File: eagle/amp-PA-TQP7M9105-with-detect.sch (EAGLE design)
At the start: 44 parts, among them J1 142-0701-851, J2 142-0701-851, Q1 P-CH, Q2 N-CH, U1 TQP7M9105, U2 BDCN-20-13+, U3 LT5534, U4 LT5534

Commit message: Update UHF PA board
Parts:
- added JP6: NP, oresat-rcl:R-US_0603-B-NOSILK
- added R9: 0, oresat-rcl:R-US_0603-B-NOSILK
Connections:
- removed net N$10: JP1.2, R7.2, U3.EN, U4.EN
- new net N$11: JP1.2, R7.2, R9.2
- new net N$14: JP6.2, R9.1, U3.EN, U4.EN
- net N$25: now also JP6.1
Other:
- note added: "2"
- note added: "Jumper"
- note added: "Optional LPF Refer to LT5534 datasheet"
- note added: "Thermal connection to ground planes are required. Dissipates up to 1W of heat."
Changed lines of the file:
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@@
 <part name="JP2" library="pinhead" library_urn="urn:adsk.eagle:library:325" deviceset="PINHD-1X3" device="" package3d_urn="urn:adsk.eagle:package:22458/2"/>
 <part name="GND11" library="supply1" library_urn="urn:adsk.eagle:library:371" deviceset="GND" device=""/>
+<part name="JP6" library="oresat-rcl" deviceset="R-US_" device="0603-B-NOSILK" value="NP"/>
+<part name="R9" library="oresat-rcl" deviceset="R-US_" device="0603-B-NOSILK" value="0"/>
 </parts>
 <sheets>
@@
 <text x="21.59" y="187.96" size="1.778" layer="97" align="bottom-right">5.0V
 External</text>
+<text x="185.42" y="170.18" size="1.778" layer="97">Optional LPF
+Refer to LT5534 datasheet</text>
+<text x="58.42" y="26.67" size="1.778" layer="97">Thermal connection to ground
+planes are required.  Dissipates
+up to 1W of heat.</text>
+<wire x1="81.28" y1="194.31" x2="99.06" y2="194.31" width="0.1524" layer="97" style="shortdash"/>
+<wire x1="99.06" y1="194.31" x2="99.06" y2="176.53" width="0.1524" layer="97" style="shortdash"/>
+<wire x1="99.06" y1="176.53" x2="81.28" y2="176.53" width="0.1524" layer="97" style="shortdash"/>
+<wire x1="81.28" y1="176.53" x2="81.28" y2="194.31" width="0.1524" layer="97" style="shortdash"/>
+<text x="82.55" y="191.77" size="1.778" layer="97">Jumper</text>
+<text x="95.25" y="190.5" size="1.778" layer="97">1</text>
+<text x="83.82" y="182.88" size="1.778" layer="97">2</text>
 </plain>
 <instances>
@@
 </instance>
 <instance part="JP4" gate="G$1" x="46.99" y="190.5" smashed="yes" rot="R180">
-<attribute name="NAME" x="54.61" y="184.785" size="1.778" layer="95" rot="R180"/>
+<attribute name="NAME" x="54.61" y="179.705" size="1.778" layer="95" rot="R180"/>
 <attribute name="VALUE" x="53.34" y="195.58" size="1.778" layer="96" rot="R180"/>
 </instance>
@@
 <instance part="GND11" gate="1" x="133.35" y="184.15" smashed="yes">
 <attribute name="VALUE" x="130.81" y="181.61" size="1.778" layer="96"/>
+</instance>
+<instance part="JP6" gate="R" x="88.9" y="181.61" smashed="yes">
+<attribute name="NAME" x="82.55" y="188.1886" size="1.778" layer="95"/>
+<attribute name="VALUE" x="85.09" y="178.308" size="1.778" layer="96"/>
+</instance>
+<instance part="R9" gate="R" x="93.98" y="186.69" smashed="yes" rot="R90">
+<attribute name="VALUE" x="97.282" y="182.88" size="1.778" layer="96" rot="R90"/>
 </instance>
 </instances>
@@
 <wire x1="101.6" y1="161.29" x2="129.54" y2="161.29" width="0.1524" layer="91"/>
 <junction x="129.54" y="161.29"/>
-</segment>
-</net>
-<net name="N$10" class="0">
-<segment>
-<pinref part="U3" gate="G$1" pin="EN"/>
-<wire x1="116.84" y1="186.69" x2="116.84" y2="168.91" width="0.1524" layer="91"/>
-<wire x1="116.84" y1="168.91" x2="147.32" y2="168.91" width="0.1524" layer="91"/>
-<wire x1="116.84" y1="168.91" x2="116.84" y2="134.62" width="0.1524" layer="91"/>
-<wire x1="116.84" y1="134.62" x2="170.18" y2="134.62" width="0.1524" layer="91"/>
-<junction x="116.84" y="168.91"/>
-<pinref part="U4" gate="G$1" pin="EN"/>
-<wire x1="170.18" y1="134.62" x2="170.18" y2="123.19" width="0.1524" layer="91"/>
-<wire x1="170.18" y1="123.19" x2="175.26" y2="123.19" width="0.1524" layer="91"/>
-<pinref part="R7" gate="R" pin="2"/>
-<wire x1="121.92" y1="185.42" x2="121.92" y2="186.69" width="0.1524" layer="91"/>
-<wire x1="121.92" y1="186.69" x2="116.84" y2="186.69" width="0.1524" layer="91"/>
-<pinref part="JP1" gate="A" pin="2"/>
-<wire x1="133.35" y1="193.04" x2="116.84" y2="193.04" width="0.1524" layer="91"/>
-<wire x1="116.84" y1="193.04" x2="116.84" y2="186.69" width="0.1524" layer="91"/>
-<junction x="116.84" y="186.69"/>
 </segment>
 </net>
@@
 <wire x1="60.96" y1="87.63" x2="60.96" y2="88.9" width="0.1524" layer="91"/>
 <pinref part="JP2" gate="A" pin="2"/>
-<wire x1="36.83" y1="88.9" x2="60.96" y2="88.9" width="0.1524" layer="91"/>
+<wire x1="36.83" y1="88.9" x2="58.42" y2="88.9" width="0.1524" layer="91"/>
 <junction x="60.96" y="88.9"/>
-</segment>
-</net>
+<pinref part="JP6" gate="R" pin="1"/>
+<wire x1="58.42" y1="88.9" x2="60.96" y2="88.9" width="0.1524" layer="91"/>
+<wire x1="83.82" y1="181.61" x2="58.42" y2="181.61" width="0.1524" layer="91"/>
+<wire x1="58.42" y1="181.61" x2="58.42" y2="88.9" width="0.1524" layer="91"/>
+<junction x="58.42" y="88.9"/>
+</segment>
+</net>
+<net name="N$11" class="0">
+<segment>
+<pinref part="JP1" gate="A" pin="2"/>
+<wire x1="133.35" y1="193.04" x2="121.92" y2="193.04" width="0.1524" layer="91"/>
+<pinref part="R9" gate="R" pin="2"/>
+<wire x1="121.92" y1="193.04" x2="93.98" y2="193.04" width="0.1524" layer="91"/>
+<wire x1="93.98" y1="191.77" x2="93.98" y2="193.04" width="0.1524" layer="91"/>
+<pinref part="R7" gate="R" pin="2"/>
+<wire x1="121.92" y1="185.42" x2="121.92" y2="193.04" width="0.1524" layer="91"/>
+<junction x="121.92" y="193.04"/>
+</segment>
+</net>
+<net name="N$14" class="0">
+<segment>
+<wire x1="93.98" y1="182.88" x2="93.98" y2="181.61" width="0.1524" layer="91"/>
+<pinref part="JP6" gate="R" pin="2"/>
+<pinref part="R9" gate="R" pin="1"/>
+<wire x1="93.98" y1="181.61" x2="93.98" y2="182.88" width="0.1524" layer="91"/>
+<pinref part="U3" gate="G$1" pin="EN"/>
+<wire x1="116.84" y1="181.61" x2="116.84" y2="168.91" width="0.1524" layer="91"/>
+<wire x1="116.84" y1="168.91" x2="147.32" y2="168.91" width="0.1524" layer="91"/>
+<wire x1="116.84" y1="168.91" x2="116.84" y2="134.62" width="0.1524" layer="91"/>
+<wire x1="116.84" y1="134.62" x2="170.18" y2="134.62" width="0.1524" layer="91"/>
+<junction x="116.84" y="168.91"/>
+<pinref part="U4" gate="G$1" pin="EN"/>
+<wire x1="170.18" y1="134.62" x2="170.18" y2="123.19" width="0.1524" layer="91"/>
+<wire x1="170.18" y1="123.19" x2="175.26" y2="123.19" width="0.1524" layer="91"/>
+<wire x1="93.98" y1="181.61" x2="116.84" y2="181.61" width="0.1524" layer="91"/>
+<junction x="93.98" y="181.61"/>
+</segment>
+</net>

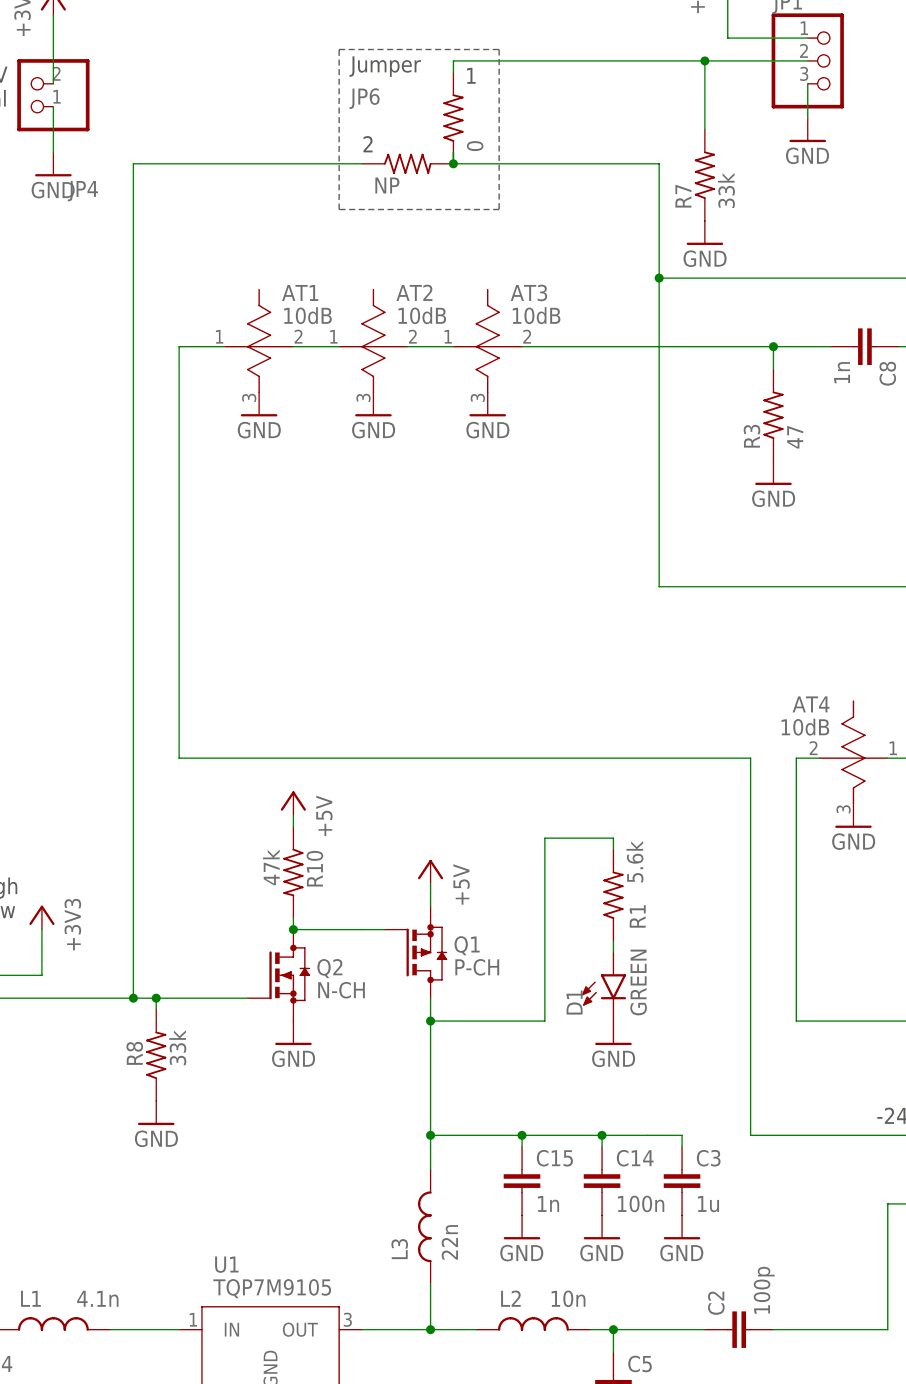
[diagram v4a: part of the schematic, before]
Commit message: Update PA TQP7M9105 values
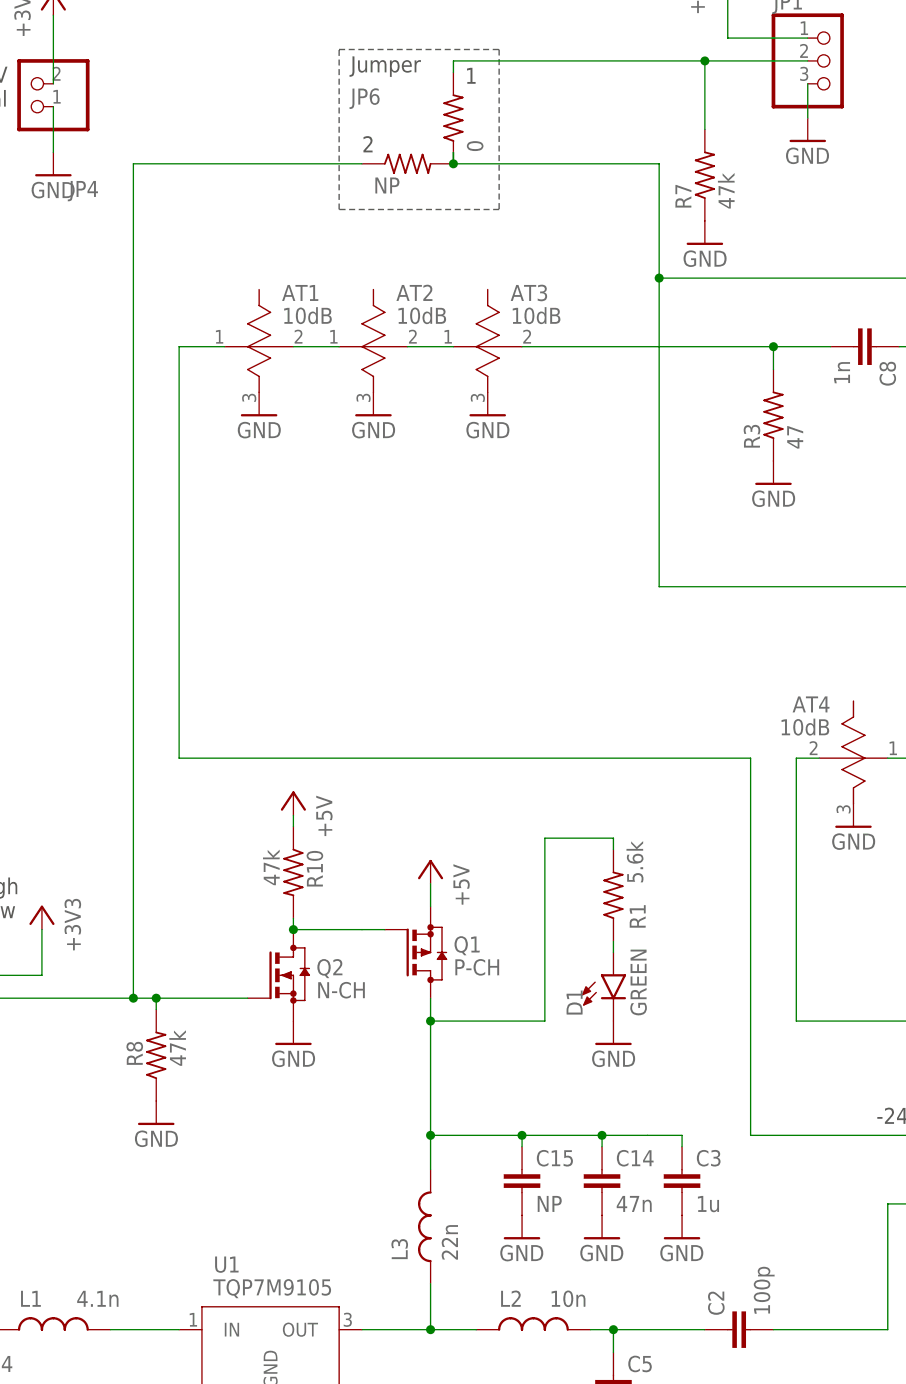
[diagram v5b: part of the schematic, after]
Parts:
- C14: value 100n -> 47n
- C15: value 1n -> NP
- R7, R8: value 33k -> 47k
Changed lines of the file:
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@@
 <part name="C13" library="oresat-rcl" deviceset="C-EU" device="0603-B-NOSILK" value="NP"/>
 <part name="GND22" library="supply1" library_urn="urn:adsk.eagle:library:371" deviceset="GND" device=""/>
-<part name="R7" library="oresat-rcl" deviceset="R-US_" device="0402-B-NOSILK" value="33k"/>
+<part name="R7" library="oresat-rcl" deviceset="R-US_" device="0402-B-NOSILK" value="47k"/>
 <part name="GND23" library="supply1" library_urn="urn:adsk.eagle:library:371" deviceset="GND" device=""/>
 <part name="Q1" library="transistor-small-signal" library_urn="urn:adsk.eagle:library:401" deviceset="BSS84" device="" package3d_urn="urn:adsk.eagle:package:28738/2" value="P-CH"/>
@@
 <part name="GND24" library="supply1" library_urn="urn:adsk.eagle:library:371" deviceset="GND" device=""/>
 <part name="P+3" library="supply1" library_urn="urn:adsk.eagle:library:371" deviceset="+5V" device=""/>
-<part name="R8" library="oresat-rcl" deviceset="R-US_" device="0402-B-NOSILK" value="33k"/>
+<part name="R8" library="oresat-rcl" deviceset="R-US_" device="0402-B-NOSILK" value="47k"/>
 <part name="GND25" library="supply1" library_urn="urn:adsk.eagle:library:371" deviceset="GND" device=""/>
 <part name="C3" library="oresat-rcl" deviceset="C-EU" device="0603-B-NOSILK" value="1u"/>
-<part name="C14" library="oresat-rcl" deviceset="C-EU" device="0603-B-NOSILK" value="100n"/>
-<part name="C15" library="oresat-rcl" deviceset="C-EU" device="0603-B-NOSILK" value="1n"/>
+<part name="C14" library="oresat-rcl" deviceset="C-EU" device="0603-B-NOSILK" value="47n"/>
+<part name="C15" library="oresat-rcl" deviceset="C-EU" device="0603-B-NOSILK" value="NP"/>
 <part name="GND5" library="supply1" library_urn="urn:adsk.eagle:library:371" deviceset="GND" device=""/>
 <part name="GND4" library="supply1" library_urn="urn:adsk.eagle:library:371" deviceset="GND" device=""/>
